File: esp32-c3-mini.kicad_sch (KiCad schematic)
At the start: 14 parts, among them J3 USB_C_Receptacle_USB2.0_16P, J4 Qwiic, SW4 RESET, SW5 SELECT, U4 ESP32-C3-MINI-1

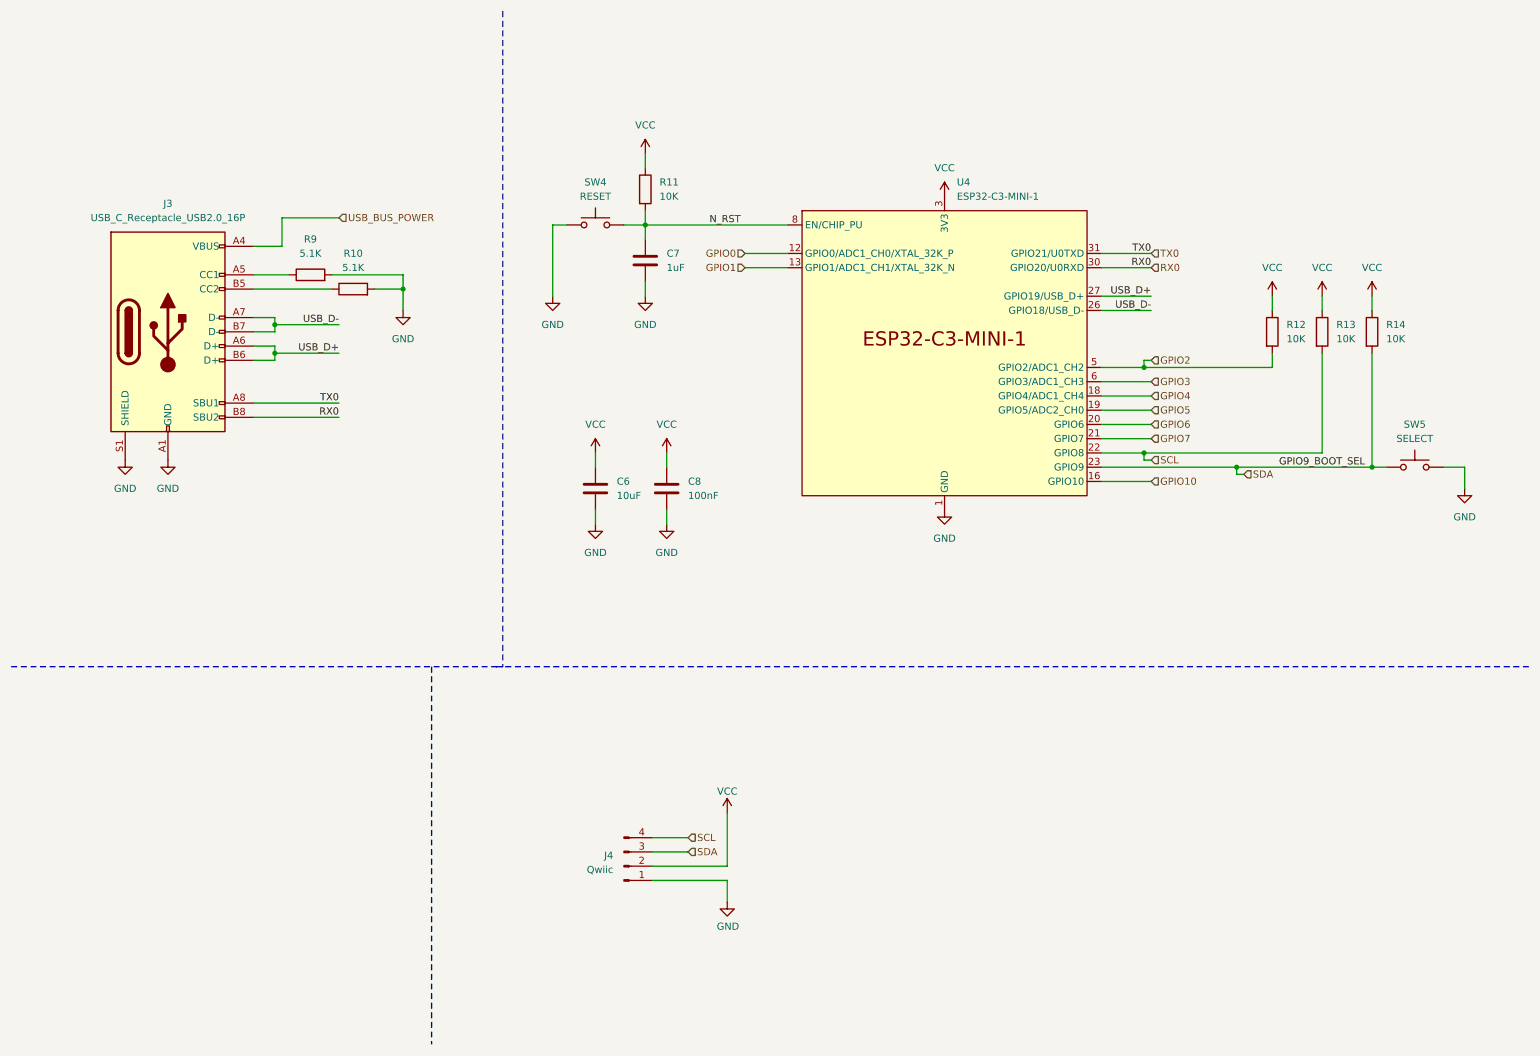
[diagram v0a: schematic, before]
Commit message: Added front artwork and token on the back
Also:
- Tweaked the trace to the antenna to hopefully better match 50ohm impedance
- Tweaked all traces to use fillet on all corners
- Added/fixed parts information

Signed-off-by: Thomas Flummer <tf@flummer.net>
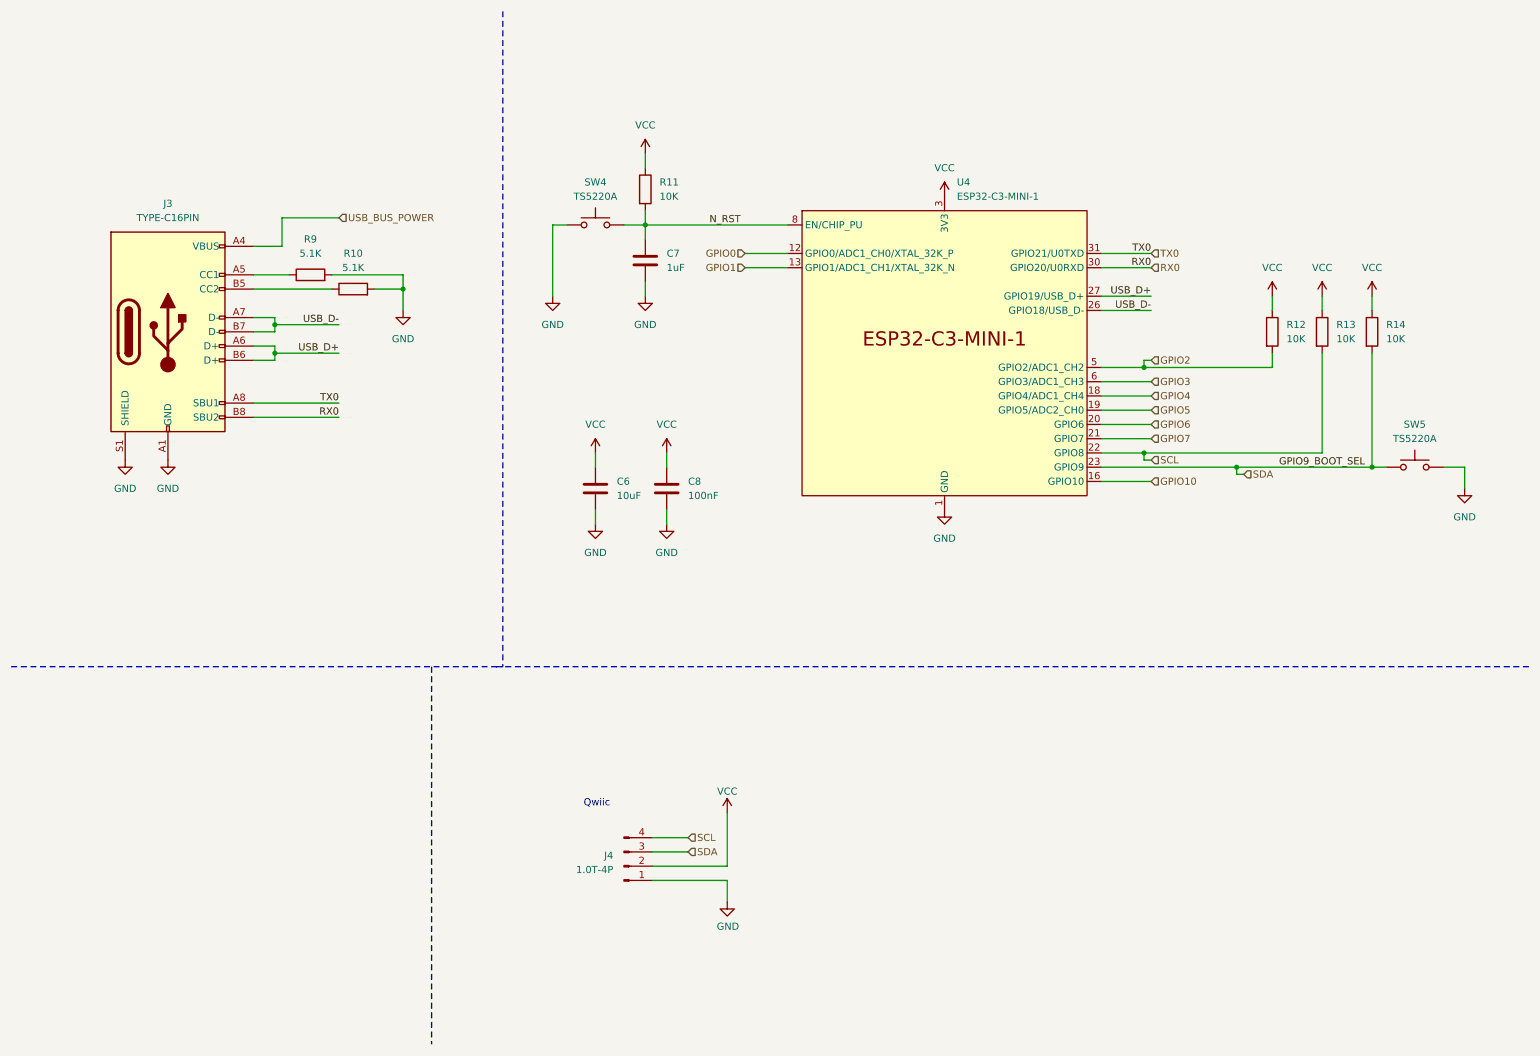
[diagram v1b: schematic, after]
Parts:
- J3: value USB_C_Receptacle_USB2.0_16P -> TYPE-C16PIN; LCSC (none) -> C393939
- J4: value Qwiic -> 1.0T-4P; LCSC (none) -> C145956
- SW4: value RESET -> TS5220A; LCSC (none) -> C412370
- SW5: value SELECT -> TS5220A; LCSC (none) -> C412370
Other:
- note added: "Qwiic"
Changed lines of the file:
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@@
 		(company "BornHack")
+	)
+	(text "Qwiic"
+		(exclude_from_sim no)
+		(at 118.364 153.924 0)
+		(effects
+			(font
+				(size 1.27 1.27)
+			)
+		)
 	)
 	(junction
@@
 			)
 		)
-		(property "Value" "USB_C_Receptacle_USB2.0_16P"
+		(property "Value" "TYPE-C16PIN"
 			(at 41.91 49.53 0)
 			(effects
@@
 			)
 		)
-		(property "Datasheet" "https://www.usb.org/sites/default/files/documents/usb_type-c.zip"
+		(property "Datasheet" "https://www.lcsc.com/datasheet/lcsc_datasheet_1912111437_SHOU-HAN-TYPE-C16PIN_C393939.pdf"
 			(at 45.72 69.85 0)
 			(effects
@@
 		)
 		(property "Description" "USB 2.0-only 16P Type-C Receptacle connector"
+			(at 41.91 69.85 0)
+			(effects
+				(font
+					(size 1.27 1.27)
+				)
+				(hide yes)
+			)
+		)
+		(property "LCSC" "C393939"
 			(at 41.91 69.85 0)
 			(effects
@@
 			)
 		)
-		(property "Value" "RESET"
+		(property "Value" "TS5220A"
 			(at 118.11 45.72 0)
 			(effects
@@
 			)
 		)
-		(property "Datasheet" "~"
+		(property "Datasheet" "https://www.lcsc.com/datasheet/lcsc_datasheet_2409272203_SHOU-HAN-TS5220A_C412370.pdf"
 			(at 118.11 45.72 0)
 			(effects
@@
 		)
 		(property "Description" "Push button switch, generic, two pins"
+			(at 118.11 50.8 0)
+			(effects
+				(font
+					(size 1.27 1.27)
+				)
+				(hide yes)
+			)
+		)
+		(property "LCSC" "C412370"
 			(at 118.11 50.8 0)
 			(effects
@@
 			)
 		)
-		(property "Value" "SELECT"
+		(property "Value" "TS5220A"
 			(at 264.16 88.9 0)
 			(effects
@@
 			)
 		)
-		(property "Datasheet" "~"
+		(property "Datasheet" "https://www.lcsc.com/datasheet/lcsc_datasheet_2409272203_SHOU-HAN-TS5220A_C412370.pdf"
 			(at 264.16 88.9 0)
 			(effects
@@
 		)
 		(property "Description" "Push button switch, generic, two pins"
+			(at 264.16 93.98 0)
+			(effects
+				(font
+					(size 1.27 1.27)
+				)
+				(hide yes)
+			)
+		)
+		(property "LCSC" "C412370"
 			(at 264.16 93.98 0)
 			(effects
@@
 			)
 		)
-		(property "Value" "Qwiic"
+		(property "Value" "1.0T-4P"
 			(at 121.285 165.7349 0)
 			(effects
@@
 			)
 		)
-		(property "Datasheet" "~"
+		(property "Datasheet" "https://www.lcsc.com/datasheet/lcsc_datasheet_2304140030_BOOMELE-Boom-Precision-Elec-1-0T-4P_C145956.pdf"
 			(at 123.19 165.1 0)
 			(effects
@@
 			)
 		)
-		(property "Description" ""
+		(property "Description" "1x4P 4P SH 4 1 1mm Surface Mount SMD,P=1mm"
 			(at 123.19 165.1 0)
 			(effects
+				(font
+					(size 1.27 1.27)
+				)
+				(hide yes)
+			)
+		)
+		(property "LCSC" "C145956"
+			(at 123.19 165.1 0)
+			(effects
